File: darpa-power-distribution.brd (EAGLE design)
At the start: 100 x 50 mm, 78 parts, among them J1 61300211121, Q1 IRFR5305, Q2 IRFR5305, Q3 IRFR5305, X1 MKDSN1,5/2-5,08, X10 MKDSN1,5/2-5,08, X2 MKDSN1,5/2-5,08, X3 MKDSN1,5/2-5,08, X4 MKDSN1,5/2-5,08, X5 MKDSN1,5/2-5,08, X6 MKDSN1,5/2-5,08, X7 MKDSN1,5/2-5,08, X8 MKDSN1,5/2-5,08, X9 MKDSN1,5/2-5,08

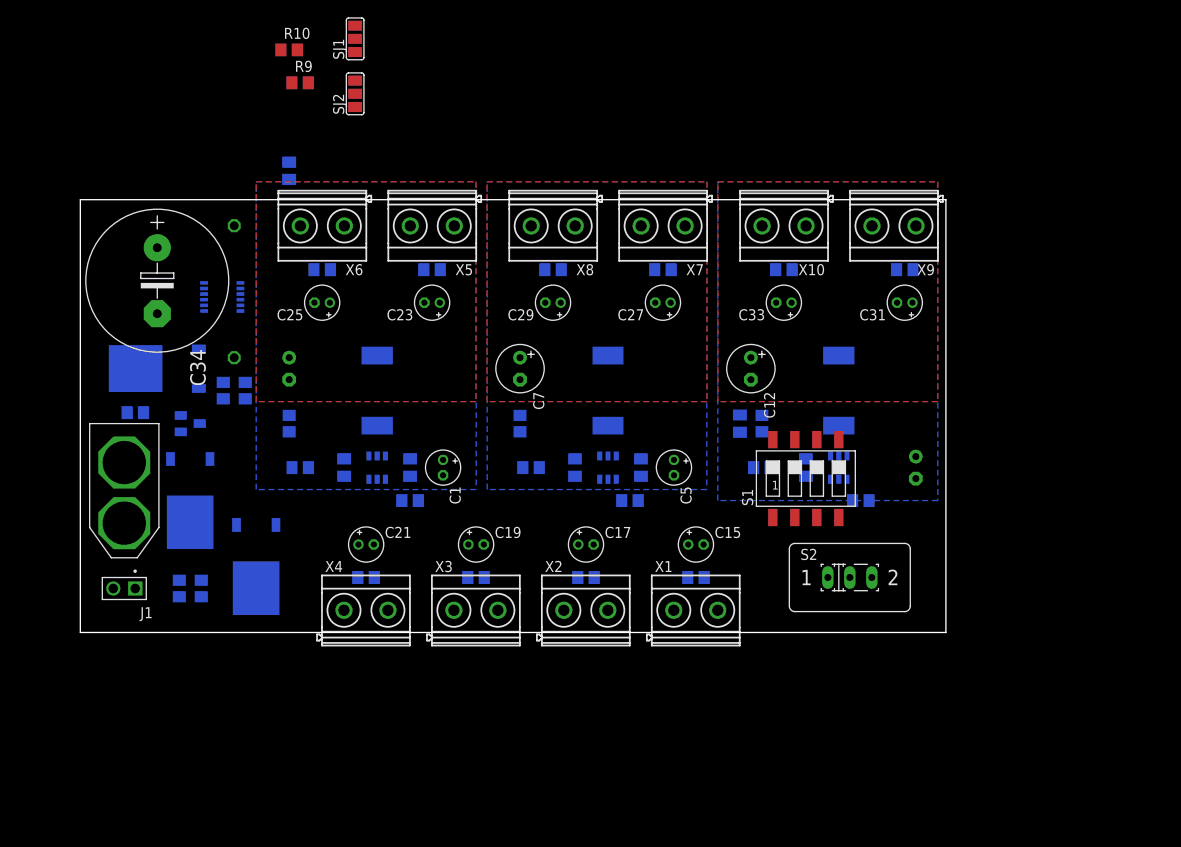
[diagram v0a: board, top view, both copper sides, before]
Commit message: placing improved. routing proceeded
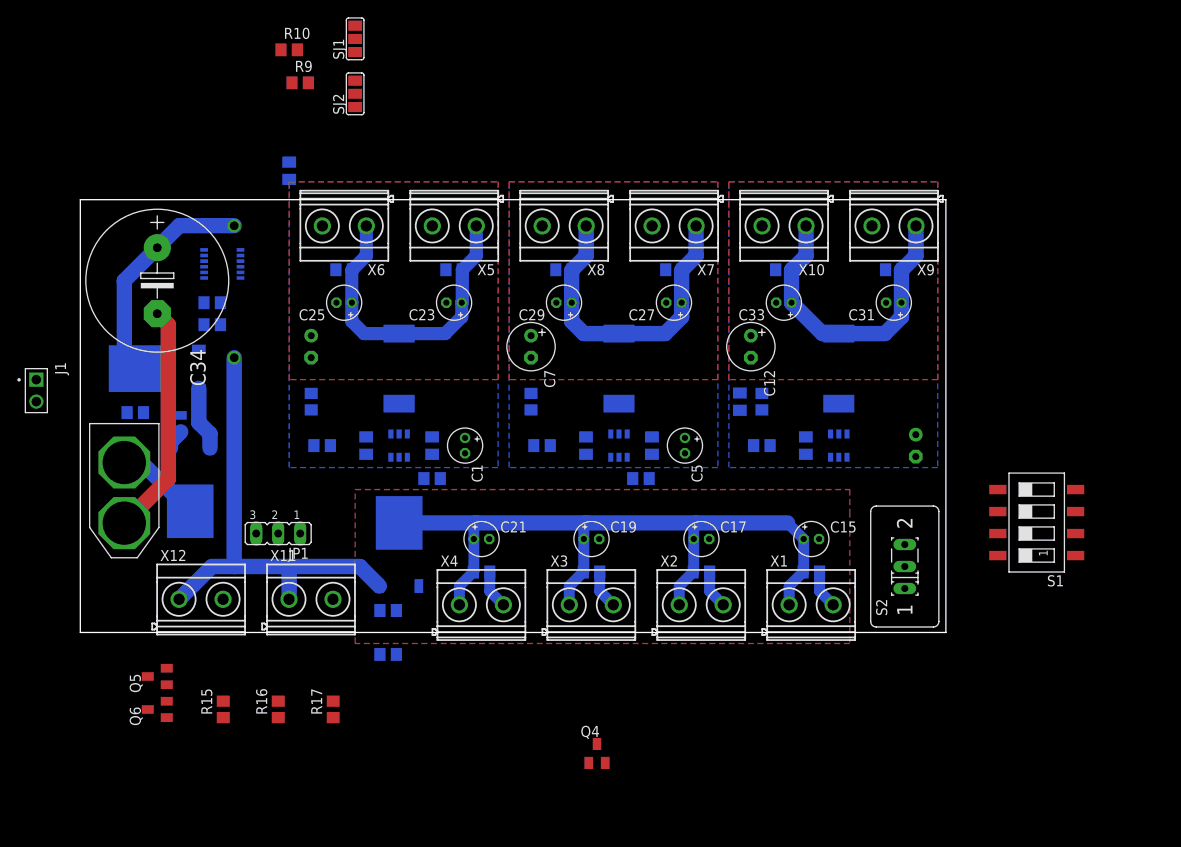
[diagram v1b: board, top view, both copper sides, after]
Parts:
- added JP1: (no value), jumper:JP2
- added Q4, Q5, Q6: BSS123, transistor-small-signal:SOT23
- added R15, R16: 470, rcl:R0805
- added X11, X12: MKDSN1,5/2-5,08, con-phoenix-508:MKDSN1,5/2-5,08
- R17: value 10k -> 470
- moved R17 65.6 mm to (29.2, -8.89), flipped to the top, turned to 90 degrees
- moved S1 27.1 mm to (110.5, 12.7), turned to 90 degrees
- moved R14 25.3 mm to (35.6, -2.54), turned to 180 degrees
- moved J1 25.0 mm to (-5.08, 27.9), turned to 270 degrees
- moved R13 21.7 mm to (35.6, 2.54), turned to 0 degrees
- moved Q3 16.7 mm to (36.8, 10.2), turned to 0 degrees
- moved C18 13.4 mm to (59.1, 6.99)
- moved C19 13.4 mm to (59.1, 10.8)
- moved X3 13.4 mm to (59.1, 3.17)
- moved C14 13.4 mm to (84.5, 6.99)
- moved C15 13.4 mm to (84.5, 10.8)
- moved C16 13.4 mm to (71.8, 6.99)
- moved C17 13.4 mm to (71.8, 10.8)
- moved C20 13.4 mm to (46.4, 6.99)
- moved C21 13.4 mm to (46.4, 10.8)
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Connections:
- new net N$16: Q5.1, R17.1
- new net N$19: Q4.1, R15.1
- new net N$21: JP1.3, R15.2
- new net N$22: JP1.1, R16.2
- new net N$23: Q6.1, R16.1
- new net N$8: JP1.2, R17.2
- net EN_6V: now also Q6.3
- net EN_MOTORS: now also Q4.3
- net EN_UDOO: now also Q5.3; no longer R17.2
- net GND: now also Q4.2, Q5.2, Q6.2, X11.2, X12.2
- net VDD: now also X11.1, X12.1; no longer R17.1
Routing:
- net MOTORS: track 0.00 -> 86.6 mm
- net VDD: track 0.00 -> 53.6 mm
- net GND: track 0.00 -> 44.6 mm
- net 6V_SERVO: track 0.00 -> 37.0 mm
- net +5V: track 0.00 -> 37.0 mm
- net 12V_UDOO: track 0.00 -> 35.7 mm
- net BATTERY: track 0.00 -> 26.0 mm
- net N$15: track 0.00 -> 9.95 mm
- net N$12: track 0.00 -> 7.42 mm
- net N$6: track 0.00 -> 2.36 mm

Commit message: proceeded routing. changes in positioning
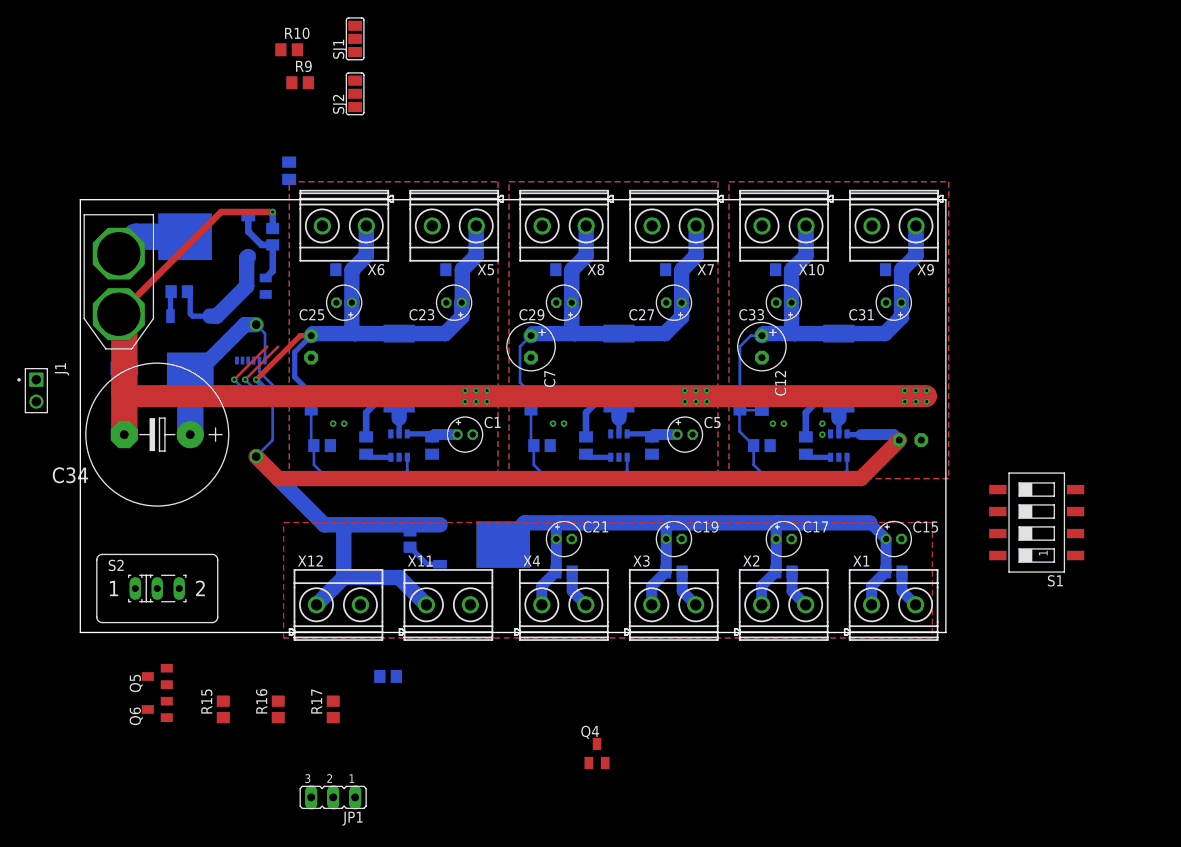
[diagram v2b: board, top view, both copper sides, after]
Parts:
- moved S2 86.4 mm to (8.89, 5.08), turned to 0 degrees
- moved JP1 31.1 mm to (29.2, -19.1)
- moved Q1 29.3 mm to (14.6, 45.7), turned to 270 degrees
- moved R7 25.8 mm to (22.2, 45.7), turned to 270 degrees
- moved U$4 24.1 mm to (4.45, 48.3)
- moved U$3 18.0 mm to (21.6, 26.7), turned to 0 degrees
- moved C34 17.8 mm to (8.89, 22.9), turned to 180 degrees
- moved D1 17.6 mm to (20.3, 40.0), turned to 270 degrees
- moved X11 15.9 mm to (42.5, 3.17)
- moved X12 15.9 mm to (29.8, 3.17)
- moved R12 12.7 mm to (5.08, 30.5), turned to 180 degrees
- moved R8 11.7 mm to (20.3, 27.9)
- moved C14 9.53 mm to (94.0, 6.99)
- moved C15 9.53 mm to (94.0, 10.8)
- moved C16 9.53 mm to (81.3, 6.99)
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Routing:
- net GND: track 44.6 -> 149.8 mm, vias 0 -> 25
- net VDD: track 53.6 -> 154.7 mm
- net +5V: track 37.0 -> 62.9 mm, vias 0 -> 1
- net N$20: track 0.00 -> 22.4 mm
- net N$7: track 0.00 -> 19.3 mm
- net N$1: track 0.00 -> 19.3 mm
- net 12V_UDOO: track 35.7 -> 52.6 mm
- net 6V_SERVO: track 37.0 -> 50.5 mm
- net N$18: track 0.00 -> 10.5 mm
- net N$3: track 0.00 -> 10.5 mm
- net N$4: track 0.00 -> 10.5 mm
- net N$10: track 0.00 -> 8.23 mm, vias 0 -> 1
- net N$9: track 0.00 -> 7.79 mm, vias 0 -> 1
- net N$12: track 7.42 -> 14.5 mm
- net N$6: track 2.36 -> 9.29 mm
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
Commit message: proceed routing
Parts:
- moved R16 104.0 mm to (121.9, 22.9), flipped to the bottom
- moved R15 103.5 mm to (116.8, 16.5), flipped to the bottom
- moved JP1 95.5 mm to (121.9, 3.81), turned to 90 degrees
- moved R17 88.2 mm to (115.6, 8.89), flipped to the bottom
- moved Q5 86.6 mm to (92.7, 16.5), flipped to the bottom, turned to 270 degrees
- moved S1 80.3 mm to (30.5, 19.1), turned to 180 degrees
- moved Q6 64.9 mm to (68.6, 16.5), flipped to the bottom, turned to 270 degrees
- moved SJ1 37.5 mm to (14.0, 35.6), turned to 270 degrees
- moved SJ2 34.3 mm to (10.2, 35.6), turned to 270 degrees
- moved Q4 33.0 mm to (47.0, 16.5), flipped to the bottom, turned to 270 degrees
- moved C8 28.3 mm to (19.7, 25.4), turned to 0 degrees
- moved R10 26.8 mm to (21.6, 40.6)
- moved R9 25.7 mm to (21.6, 38.1)
- moved J1 23.4 mm to (14.6, 40.6), turned to 180 degrees
- moved R14 21.4 mm to (42.2, 15.2)
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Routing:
- net EN_UDOO: track 0.00 -> 61.3 mm, vias 0 -> 1
- net GND: track 149.8 -> 205.5 mm, vias 25 -> 31
- net EN_6V: track 0.00 -> 45.2 mm, vias 0 -> 1
- net +5V: track 62.9 -> 88.2 mm
- net SCL: track 0.00 -> 21.8 mm, vias 0 -> 1
- net EN_5V: track 0.00 -> 16.1 mm, vias 0 -> 1
- net EN_MOTORS: track 0.00 -> 14.2 mm, vias 0 -> 1
- net SDA: track 0.00 -> 13.7 mm, vias 0 -> 1
- net N$13: track 4.27 -> 12.3 mm
- net N$10: track 8.23 -> 16.1 mm
- net VDD: track 154.7 -> 162.3 mm, vias 0 -> 2
- net N$9: track 7.79 -> 15.3 mm
- net N$7: track 19.3 -> 22.0 mm
- net N$1: track 19.3 -> 22.0 mm
- net N$20: track 22.4 -> 25.1 mm
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
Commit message: routing completed; Errors fixed; added LEDs and BOM; TODO: DRC, second cheack and approval
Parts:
- added LED1, LED2, LED3, LED4: (no value), led:SML0805
- added R20, R23: 600, rcl:R0805
- added R21, R22: 200, rcl:R0805
- C14, C16, C18, C20, C22, C24, C26, C28, C30, C32: device rcl:C0805 -> rcl:C0805K
- moved R16 49.9 mm to (72.4, 17.1), turned to 180 degrees
- moved R15 49.5 mm to (67.3, 15.2), turned to 180 degrees
- moved JP1 27.1 mm to (95.9, 11.4), turned to 270 degrees
- moved R17 23.6 mm to (93.7, 17.8), turned to 180 degrees
- moved C14 6.35 mm to (87.6, 6.99)
- moved C15 6.35 mm to (87.6, 10.8)
- moved X1 6.35 mm to (87.6, 3.17)
- moved C18 6.35 mm to (62.2, 6.99)
- moved C19 6.35 mm to (62.2, 10.8)
- moved C20 6.35 mm to (49.5, 6.99)
- moved C21 6.35 mm to (49.5, 10.8)
- moved R13 6.35 mm to (31.8, 10.8)
- moved X11 6.35 mm to (36.2, 3.17)
- moved X3 6.35 mm to (62.2, 3.17)
- moved X4 6.35 mm to (49.5, 3.17)
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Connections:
- new net N$27: LED1.A, R20.1
- new net N$28: LED2.A, R21.1
- new net N$29: LED3.A, R22.1
- new net N$30: LED4.A, R23.1
- net +5V: now also R21.2
- net 12V_UDOO: now also R23.2
- net 6V_SERVO: now also R22.2
- net GND: now also LED1.C, LED2.C, LED3.C, LED4.C
- net N$22: now also JP1.2; no longer JP1.1
- net N$8: now also JP1.1; no longer JP1.2
- net VDD: now also R20.2
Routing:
- net GND: track 205.5 -> 282.1 mm, vias 31 -> 33
- net N$21: track 0.00 -> 30.3 mm
- net N$22: track 0.00 -> 24.9 mm
- net N$14: track 0.00 -> 23.3 mm
- net N$19: track 0.00 -> 23.0 mm
- net N$11: track 3.37 -> 11.3 mm
- net N$23: track 0.00 -> 7.55 mm
- net EN_MOTORS: track 14.2 -> 9.26 mm
- net N$27: track 0.00 -> 4.35 mm
- net N$8: track 0.00 -> 4.34 mm
- net N$16: track 0.00 -> 3.16 mm
- net 12V_UDOO: track 52.6 -> 55.5 mm
- net 6V_SERVO: track 50.5 -> 53.4 mm
- net +5V: track 88.2 -> 91.1 mm
- net VDD: track 162.3 -> 164.9 mm
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
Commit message: corrected typo in resistor value
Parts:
- R19: value 5.23 -> 5.23k
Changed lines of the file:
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@@
 <attribute name="VALUE" x="73.66" y="26.035" size="1.27" layer="28" rot="MR90"/>
 </element>
-<element name="R19" library="rcl" library_urn="urn:adsk.eagle:library:334" package="R0805" package3d_urn="urn:adsk.eagle:package:23553/2" value="5.23" x="78.74" y="21.59" smashed="yes" rot="MR0">
+<element name="R19" library="rcl" library_urn="urn:adsk.eagle:library:334" package="R0805" package3d_urn="urn:adsk.eagle:package:23553/2" value="5.23k" x="78.74" y="21.59" smashed="yes" rot="MR0">
 <attribute name="NAME" x="79.375" y="22.86" size="1.27" layer="26" rot="MR0"/>
 <attribute name="POPULARITY" value="86" x="22.86" y="-53.34" size="1.778" layer="28" rot="MR0" display="off"/>

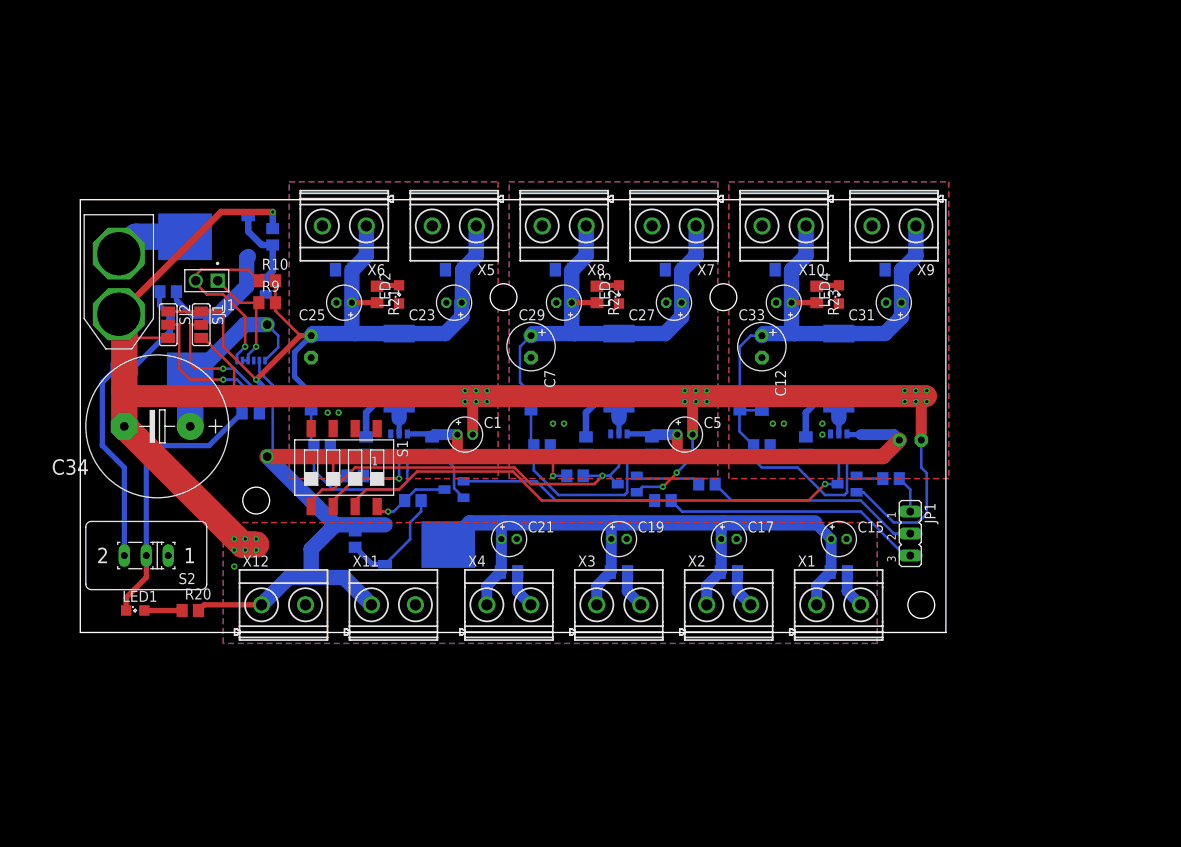
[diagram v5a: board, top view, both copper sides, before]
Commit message: placing improved, DRC done, labels aligned
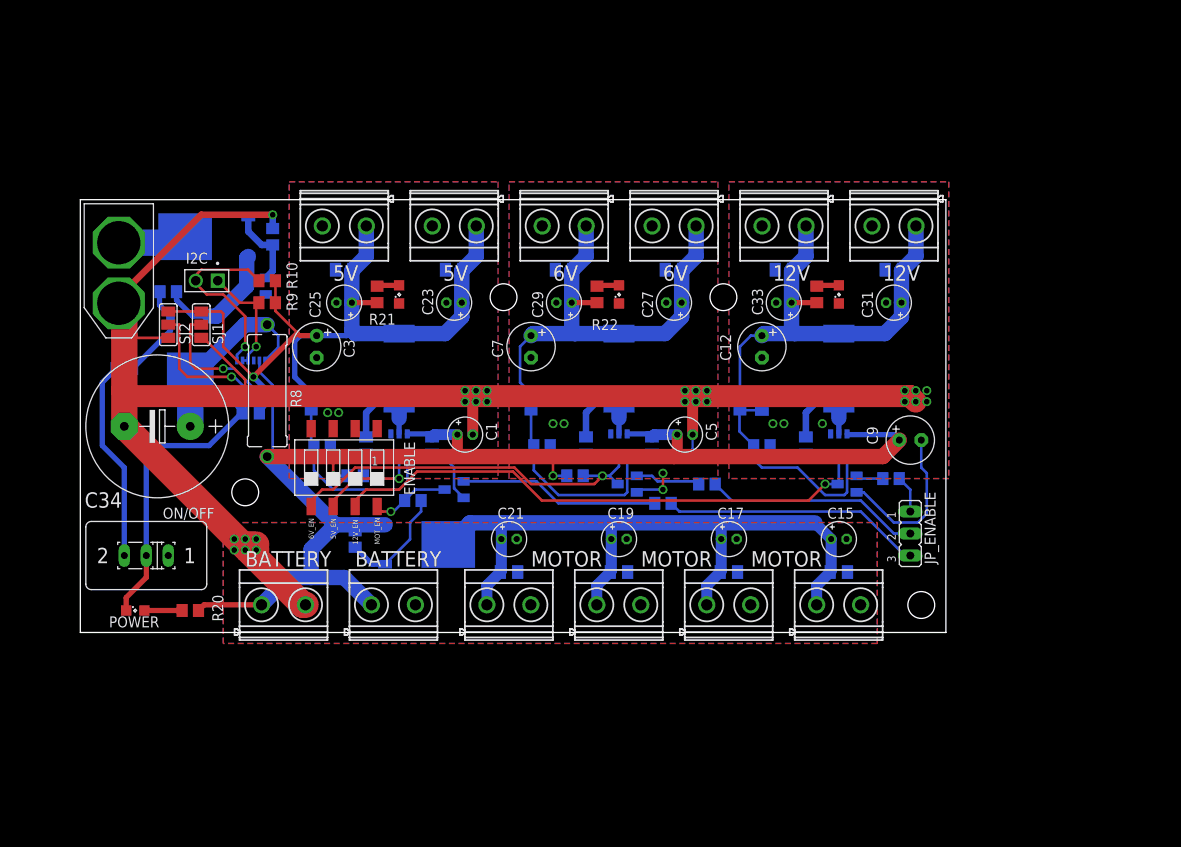
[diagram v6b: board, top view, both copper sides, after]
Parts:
- moved U$4 1.27 mm to (4.45, 49.5)
- moved C3 0.63 mm to (27.3, 33.0), flipped to the top
- moved R15 0.32 mm to (67.3, 14.9)
- flipped C9 to the top, turned to 0 degrees
- flipped R8 to the top
- renumbered J1 to I2C, JP1 to JP_ENABLE, LED1 to POWER, LED2 to 5V, LED3 to 6V, R23 to 12V, S1 to ENABLE, S2 to ON/OFF, U$1 to 5V_REG, U$2 to 6V_REG, U$5 to 12V_REG
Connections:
- net N$21 renamed JP_MOTORS
- net N$22 renamed JP_6V
- net N$8 renamed JP_12V
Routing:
- net GND: track 282.1 -> 270.5 mm, vias 33 -> 34
- net +5V: track 91.1 -> 91.9 mm
- net N$12: track 15.4 -> 14.8 mm
- net N$15: track 8.47 -> 7.95 mm
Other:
- board text added: "12V"
- board text added: "12V_EN"
- board text added: "5V"
- board text added: "5V_EN"
- board text added: "6V"
- board text added: "6V_EN"
- board text added: "BATTERY"
- board text added: "MOTOR"
- board text added: "MOT_EN"
